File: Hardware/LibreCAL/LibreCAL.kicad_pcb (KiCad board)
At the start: 2 copper layers, 94 parts, among them J1 901-10510-2, J2 901-10510-2, J3 901-10510-2, J4 901-10510-2, J5 USB_C_Receptacle_USB2.0, J6 TC2030-ARM, Q1 IRLML2060, SW1 TL3301CF160QG, SW2 TL3301CF160QG, SW3 TL3301CF160QG, U1 PE426462, U2 PE426462, U3 PE426462, U4 PE426462, U5 W25Q16JVSNIQ, U6 IP4234CZ6, U7 RP2040, U8 W25Q16JVSNIQ, U9 MIC5528-3.3YMT-TR, Y1 ECS-120-8-36-CKM-TR3

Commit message: Partial routing
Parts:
- removed R10, R11: 13, Resistor_SMD:R_2512_6332Metric
- D1, D10, D11, D2, D3, D4, D5, D6, D7, D8, D9, J6, R14, R15, R16, R17, R18, R19, R20, R21, R22, R23, R24, SW1, SW2, SW3, TH1: moved to B.Cu
- R8, R9: value 13 -> 6R2; moved to B.Cu
- moved C30 97.4 mm to (119.6, 135.3), turned to -90 degrees
- moved C32 96.7 mm to (115.8, 135.3), turned to 90 degrees
- moved C28 93.9 mm to (121.6, 135.3), turned to -90 degrees
- moved C31 93.8 mm to (116.8, 135.3), turned to 90 degrees
- moved FB2 90.5 mm to (121.6, 133.4), turned to -90 degrees
- moved U9 89.8 mm to (118.2, 135.3), turned to 90 degrees
- moved C29 89.8 mm to (120.6, 135.3), turned to -90 degrees
- moved Q1 78.3 mm to (120.7, 121.0), turned to 180 degrees
- moved D6 76.8 mm to (109.0, 113.0), turned to 90 degrees
- moved C27 76.7 mm to (121.2, 123.7), turned to -90 degrees
- moved R18 75.4 mm to (115.0, 113.8)
- moved R19 74.7 mm to (111.0, 113.8)
- moved D7 73.8 mm to (105.0, 113.0), turned to 90 degrees
- moved SW3 73.6 mm to (110.0, 129.5), turned to 90 degrees
- moved R17 71.0 mm to (119.0, 113.8)
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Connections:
- U1 pad 20: unconnected-(U1-Pad20) -> GND
- U2 pad 20: unconnected-(U2-Pad20) -> GND
- U3 pad 2: Net-(U1-Pad15) -> Net-(U2-Pad2)
- U3 pad 20: unconnected-(U3-Pad20) -> GND
- U3 pad 4: Net-(U2-Pad4) -> Net-(U1-Pad15)
- U4 pad 15: Net-(U2-Pad2) -> Net-(U2-Pad4)
- U4 pad 20: unconnected-(U4-Pad20) -> GND
- U6 pad 1: Net-(J5-PadA7) -> Net-(J5-PadA6)
- U6 pad 6: Net-(J5-PadA6) -> Net-(J5-PadA7)
- U7 pad 11: P2_V2 -> LED_PORT4
- U7 pad 12: P2_V3 -> P3_V3
- U7 pad 13: P3_V1 -> P3_V2
- U7 pad 14: P3_V2 -> P3_V1
- U7 pad 15: P3_V3 -> P4_V1
- U7 pad 16: P4_V1 -> P4_V2
- U7 pad 17: P4_V2 -> P4_V3
- U7 pad 18: P4_V3 -> P2_V3
- U7 pad 27: LED_READY -> P2_V2
- U7 pad 28: LED_WAIT -> P2_V1
- U7 pad 29: LED_OPEN -> P1_V1
- U7 pad 30: LED_SHORT -> P1_V2
- U7 pad 31: LED_LOAD -> P1_V3
- U7 pad 32: LED_THROUGH -> LED_PORT1
- U7 pad 34: LED_PORT1 -> LED_PORT3
- U7 pad 35: LED_PORT2 -> LED_OPEN
- U7 pad 36: LED_PORT3 -> LED_SHORT
- U7 pad 37: LED_PORT4 -> LED_LOAD
- U7 pad 38: ADC_TEMP -> LED_THROUGH
- U7 pad 40: BUTTON1 -> HEATER
- U7 pad 41: HEATER -> ADC_TEMP
- U7 pad 46: Net-(U6-Pad3) -> Net-(U6-Pad4)
- U7 pad 47: Net-(U6-Pad4) -> Net-(U6-Pad3)
- U7 pad 6: P1_V1 -> BUTTON1
- U7 pad 7: P1_V2 -> LED_READY
- U7 pad 8: P1_V3 -> LED_WAIT
- U7 pad 9: P2_V1 -> LED_PORT2
- Y1 pad 4: (no net) -> GND
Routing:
- net GND: track 0.00 -> 179.0 mm, vias 0 -> 886
- net +3V3: track 0.00 -> 156.4 mm, vias 0 -> 18
- net P3_V3: track 0.00 -> 80.2 mm, vias 0 -> 2
- net P3_V2: track 0.00 -> 79.9 mm, vias 0 -> 2
- net P2_V3: track 0.00 -> 68.8 mm, vias 0 -> 2
- net P1_V3: track 0.00 -> 68.1 mm, vias 0 -> 2
- net P2_V1: track 0.00 -> 67.1 mm, vias 0 -> 2
- net P2_V2: track 0.00 -> 64.8 mm, vias 0 -> 2
- net P1_V2: track 0.00 -> 63.6 mm, vias 0 -> 2
- net P1_V1: track 0.00 -> 61.8 mm, vias 0 -> 2
- net Net-(R12-Pad2): track 0.00 -> 61.0 mm, vias 0 -> 2
- net P3_V1: track 0.00 -> 53.7 mm, vias 0 -> 2
- net LED_PORT2: track 0.00 -> 48.5 mm, vias 0 -> 2
- net LED_PORT1: track 0.00 -> 46.4 mm, vias 0 -> 2
- net P4_V1: track 0.00 -> 41.9 mm, vias 0 -> 2
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- added copper zone on B.Cu, net GND
- added copper zone on F.Cu, net GND
- added copper zone on In1.Cu, net GND
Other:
- board outline added: 55 x 65.5 mm
- copper layers 2 -> 4

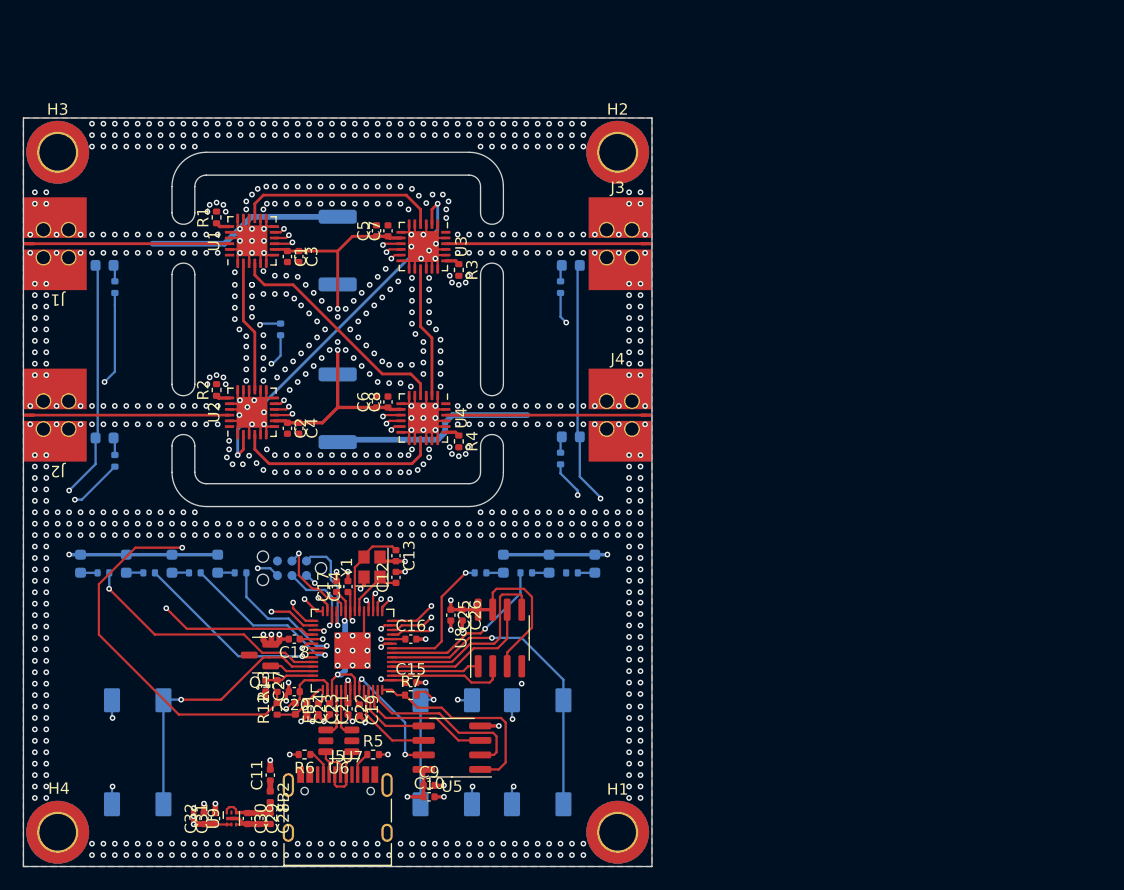
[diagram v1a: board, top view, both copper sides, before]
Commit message: Filters added, housing updated
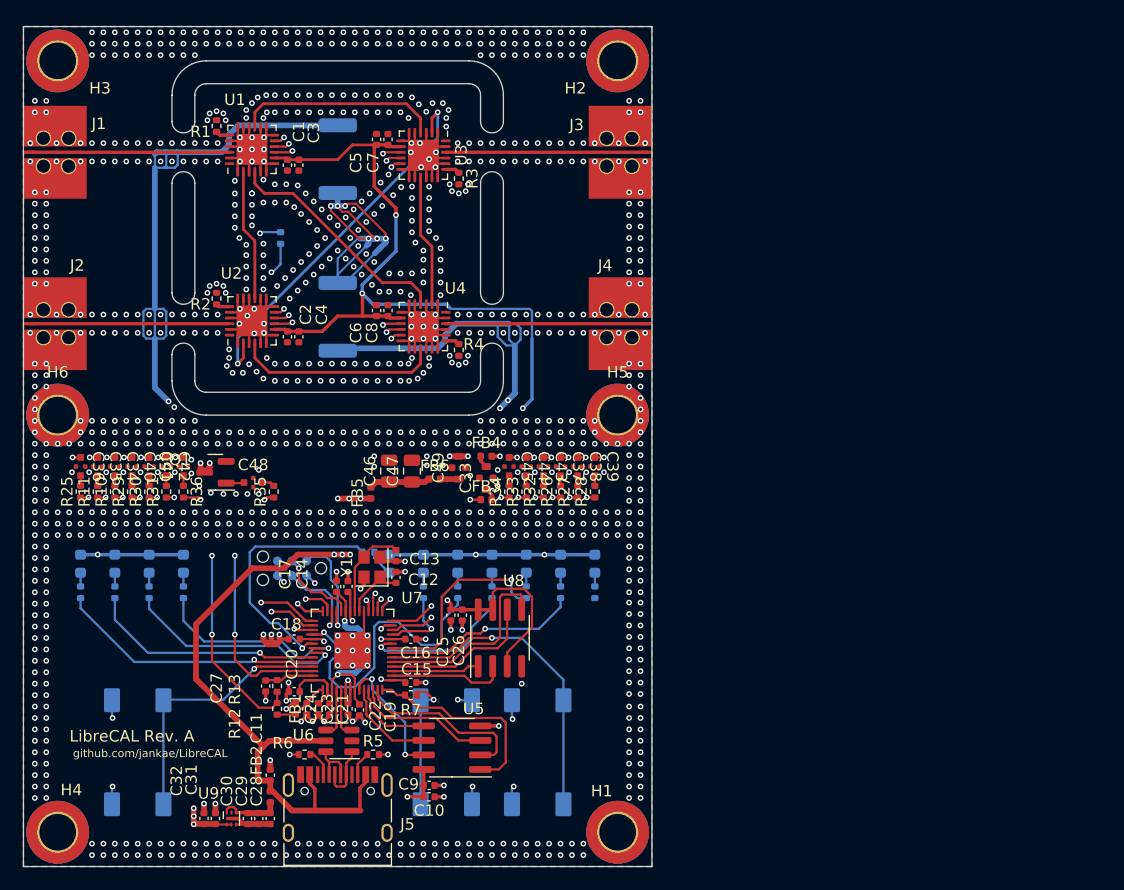
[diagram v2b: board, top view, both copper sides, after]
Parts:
- added C33: NFM21PC475B1A3D, LibreCAL:NFM21PC, F.Cu at (140.5, 105.5)
- added C34: NFM18CC223R1C3D, LibreCAL:NFM18CC, F.Cu at (108.0, 104.5)
- added C35: NFM18CC223R1C3D, LibreCAL:NFM18CC, F.Cu at (106.5, 104.5)
- added C36: NFM18CC223R1C3D, LibreCAL:NFM18CC, F.Cu at (105.0, 104.5)
- added C37: NFM18CC223R1C3D, LibreCAL:NFM18CC, F.Cu at (147.0, 104.5)
- added C38: NFM18CC223R1C3D, LibreCAL:NFM18CC, F.Cu at (148.5, 104.5)
- added C39: NFM18CC223R1C3D, LibreCAL:NFM18CC, F.Cu at (150.0, 104.5)
- added C40: NFM18CC223R1C3D, LibreCAL:NFM18CC, F.Cu at (109.5, 104.5)
- added C41: NFM18CC223R1C3D, LibreCAL:NFM18CC, F.Cu at (111.0, 104.5)
- added C42: NFM18CC223R1C3D, LibreCAL:NFM18CC, F.Cu at (112.5, 104.5)
- added C43: NFM18CC223R1C3D, LibreCAL:NFM18CC, F.Cu at (145.5, 104.5)
- added C44: NFM18CC223R1C3D, LibreCAL:NFM18CC, F.Cu at (144.0, 104.5)
- added C45: NFM18CC223R1C3D, LibreCAL:NFM18CC, F.Cu at (142.5, 104.5)
- added C46: 22u, Capacitor_SMD:C_0805_2012Metric, F.Cu at (132.0, 104.9)
- added C47: 22u, Capacitor_SMD:C_0805_2012Metric, F.Cu at (134.0, 104.9)
- added C48: NFM18CC223R1C3D, LibreCAL:NFM18CC, F.Cu at (120.1, 105.9)
- added C49: NFM21PC475B1A3D, LibreCAL:NFM21PC, F.Cu at (138.1, 104.6)
- added C50: NFM18CC223R1C3D, LibreCAL:NFM18CC, F.Cu at (114.0, 104.5)
- added COVER1: Top Cover, LibreCAL:TopCover, B.Cu at (155.0, 139.5)
- added COVER2: Bottom Cover, LibreCAL:BottomCover, B.Cu at (155.0, 139.5)
- added FB3: MMZ1005A222ET000, Inductor_SMD:L_0402_1005Metric, F.Cu at (140.5, 107.4)
- added FB4: MMZ1005A222ET000, Inductor_SMD:L_0402_1005Metric, F.Cu at (140.5, 103.6)
- added FB5: MMZ1005S121CTD25, Inductor_SMD:L_0402_1005Metric, F.Cu at (130.4, 106.8)
- added FB6: MMZ1005S121CTD25, Inductor_SMD:L_0402_1005Metric, F.Cu at (136.0, 105.6)
- added H5: MountingHole_Pad, MountingHole:MountingHole_3.2mm_M3_ISO14580_Pad_TopBottom, F.Cu at (152.0, 100.0)
- added H6: MountingHole_Pad, MountingHole:MountingHole_3.2mm_M3_ISO14580_Pad_TopBottom, F.Cu at (103.0, 100.0)
- added R10: 47k, Resistor_SMD:R_0402_1005Metric, F.Cu at (108.0, 106.7)
- added R11: 47k, Resistor_SMD:R_0402_1005Metric, F.Cu at (106.5, 106.7)
- added R25: 47k, Resistor_SMD:R_0402_1005Metric, F.Cu at (105.0, 106.7)
- added R26: 47k, Resistor_SMD:R_0402_1005Metric, F.Cu at (147.0, 106.7)
- added R27: 47k, Resistor_SMD:R_0402_1005Metric, F.Cu at (148.5, 106.7)
- added R28: 47k, Resistor_SMD:R_0402_1005Metric, F.Cu at (150.0, 106.7)
- added R29: 47k, Resistor_SMD:R_0402_1005Metric, F.Cu at (109.5, 106.7)
- added R30: 47k, Resistor_SMD:R_0402_1005Metric, F.Cu at (111.0, 106.7)
- added R31: 47k, Resistor_SMD:R_0402_1005Metric, F.Cu at (112.5, 106.7)
- added R32: 47k, Resistor_SMD:R_0402_1005Metric, F.Cu at (145.5, 106.7)
- added R33: 47k, Resistor_SMD:R_0402_1005Metric, F.Cu at (144.0, 106.7)
- added R34: 47k, Resistor_SMD:R_0402_1005Metric, F.Cu at (142.5, 106.7)
- added R35: 47k, Resistor_SMD:R_0402_1005Metric, F.Cu at (121.9, 106.7)
- added R36: 100, Resistor_SMD:R_0402_1005Metric, F.Cu at (114.0, 106.7)
- moved D8 40.4 mm to (138.0, 113.0), turned to 90 degrees
- moved R21 40.2 mm to (138.0, 115.5)
- moved R22 27.4 mm to (141.0, 115.5)
- moved D10 27.2 mm to (132.0, 113.0), turned to 90 degrees
- moved D9 27.0 mm to (141.0, 113.0), turned to 90 degrees
- moved R23 23.6 mm to (130.2, 112.0), turned to 180 degrees
- moved D11 17.0 mm to (135.0, 113.0), turned to 90 degrees
- moved R24 16.8 mm to (135.0, 115.5)
- moved Q1 16.5 mm to (116.8, 105.0)
- moved C1 8.00 mm to (123.1, 78.1)
- moved C2 8.00 mm to (123.1, 93.2)
- moved C3 8.00 mm to (124.1, 78.1)
- moved C4 8.00 mm to (124.1, 93.2)
- moved C5 8.00 mm to (130.9, 75.9)
- moved C6 8.00 mm to (130.9, 90.8)
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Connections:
- C1 pad 1: +3V3 -> Net-(C6-Pad1)
- C2 pad 1: +3V3 -> Net-(C6-Pad1)
- C3 pad 1: +3V3 -> Net-(C6-Pad1)
- C4 pad 1: +3V3 -> Net-(C6-Pad1)
- C5 pad 1: +3V3 -> Net-(C6-Pad1)
- C6 pad 1: +3V3 -> Net-(C6-Pad1)
- C7 pad 1: +3V3 -> Net-(C6-Pad1)
- C8 pad 1: +3V3 -> Net-(C6-Pad1)
- Q1 pad 1: HEATER -> Net-(Q1-Pad1)
- R12 pad 2: Net-(R12-Pad2) -> Net-(R13-Pad1)
- R13 pad 1: Net-(R12-Pad2) -> Net-(R13-Pad1)
- R21 pad 2: LED_PORT1 -> LED_PORT2
- R22 pad 2: LED_PORT2 -> LED_PORT1
- R23 pad 2: LED_PORT3 -> LED_PORT4
- R24 pad 2: LED_PORT4 -> LED_PORT3
- R8 pad 1: +5V -> Net-(R8-Pad1)
- TH1 pad 1: Net-(R12-Pad2) -> Net-(C50-Pad3)
- U1 pad 10: P1_V2 -> Net-(U1-Pad10)
- U1 pad 11: P1_V3 -> Net-(U1-Pad11)
- U1 pad 8: +3V3 -> Net-(C6-Pad1)
- U1 pad 9: P1_V1 -> Net-(U1-Pad9)
- U2 pad 10: P3_V2 -> Net-(U2-Pad10)
- U2 pad 11: P3_V3 -> Net-(U2-Pad11)
- U2 pad 8: +3V3 -> Net-(C6-Pad1)
- U2 pad 9: P3_V1 -> Net-(U2-Pad9)
- U3 pad 10: P2_V2 -> Net-(U3-Pad10)
- U3 pad 11: P2_V3 -> Net-(U3-Pad11)
- U3 pad 8: +3V3 -> Net-(C6-Pad1)
- U3 pad 9: P2_V1 -> Net-(U3-Pad9)
- U4 pad 10: P4_V2 -> Net-(U4-Pad10)
- U4 pad 11: P4_V3 -> Net-(U4-Pad11)
- U4 pad 8: +3V3 -> Net-(C6-Pad1)
- U4 pad 9: P4_V1 -> Net-(U4-Pad9)
- U7 pad 11: LED_PORT4 -> LED_PORT3
- U7 pad 12: P3_V3 -> P4_V3
- U7 pad 13: P3_V2 -> P4_V2
- U7 pad 14: P3_V1 -> P4_V1
- U7 pad 15: P4_V1 -> P3_V1
- U7 pad 16: P4_V2 -> P3_V2
- U7 pad 17: P4_V3 -> P3_V3
- U7 pad 18: P2_V3 -> P1_V3
- U7 pad 27: P2_V2 -> P1_V2
- U7 pad 28: P2_V1 -> P1_V1
- U7 pad 29: P1_V1 -> P2_V1
- U7 pad 30: P1_V2 -> P2_V2
- U7 pad 31: P1_V3 -> P2_V3
- U7 pad 32: LED_PORT1 -> LED_PORT2
- U7 pad 34: LED_PORT3 -> LED_PORT4
- U7 pad 9: LED_PORT2 -> LED_PORT1
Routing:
- net +3V3: track 156.4 -> 80.5 mm, vias 18 -> 16
- net Net-(Q1-Pad3): track 0.00 -> 73.5 mm, vias 0 -> 4
- net Net-(C6-Pad1): track 0.00 -> 71.3 mm, vias 0 -> 4
- net Net-(U2-Pad11): track 0.00 -> 63.1 mm, vias 0 -> 2
- net +5V: track 19.0 -> 81.0 mm, vias 0 -> 6
- net Net-(R12-Pad2): track 61.0 -> 0.00 mm, vias 2 -> 0
- net Net-(U2-Pad10): track 0.00 -> 60.2 mm, vias 0 -> 2
- net P3_V3: track 80.2 -> 20.3 mm
- net P3_V2: track 79.9 -> 20.3 mm
- net Net-(R8-Pad1): track 0.00 -> 51.4 mm, vias 0 -> 4
- net Net-(U3-Pad9): track 0.00 -> 49.2 mm, vias 0 -> 2
- net Net-(U3-Pad10): track 0.00 -> 46.6 mm, vias 0 -> 2
- net Net-(U1-Pad11): track 0.00 -> 46.3 mm, vias 0 -> 2
- net Net-(U3-Pad11): track 0.00 -> 45.0 mm, vias 0 -> 2
- net Net-(U1-Pad10): track 0.00 -> 44.2 mm, vias 0 -> 2
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- added copper zone on In2.Cu, net +3V3
- added copper zone on In2.Cu, net GND
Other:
- board size 55 x 65.5 mm -> 55 x 73.5 mm
- board text added: "BOOTSEL"
- board text added: "FUNCTION"
- board text added: "LOAD"
- board text added: "LibreCAL Rev. A"
- board text added: "OPEN"
- board text added: "PORT"
- board text added: "PORT1"
- board text added: "PORT2"
- board text added: "PORT3"
- board text added: "PORT4"
- board text added: "POWER"
- board text added: "READY"
- board text added: "SHORT"
- board text added: "THROUGH"
- board text added: "WAIT"
- board text added: "github.com/jankae/LibreCAL"

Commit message: Production files
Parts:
- COVER2: moved to F.Cu
- moved COVER2 57.5 mm to (97.5, 139.5), turned to 0 degrees
- moved COVER1 2.50 mm to (157.5, 139.5)
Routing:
- net GND: track 160.5 -> 172.9 mm, vias 1081 -> 1065

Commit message: replaced bootsel switch, adjusted covers
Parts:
- SW1: value TL3301CF160QG -> TL3301NF160QG; footprint LibreCAL:TL3301-J -> LibreCAL:TL3301N-J
- SW2, SW3: footprint LibreCAL:TL3301-J -> LibreCAL:TL3301C-J

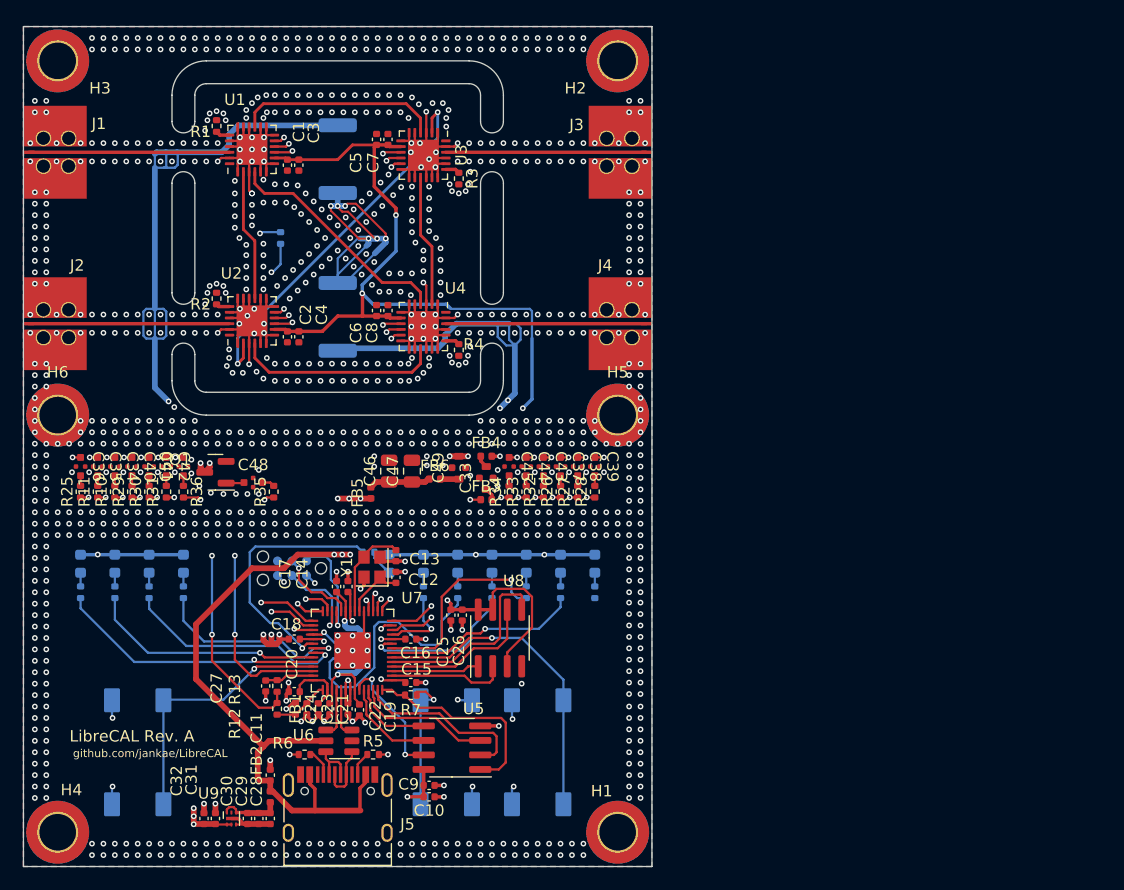
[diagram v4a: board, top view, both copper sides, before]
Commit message: Improvements on LibreCAL KiCad: fixed minor errors/labels(cosmetic), improved BOM(Added LCSC_Part), improved Impedance JLCPCB 4Layer JLC7628 1.6mm
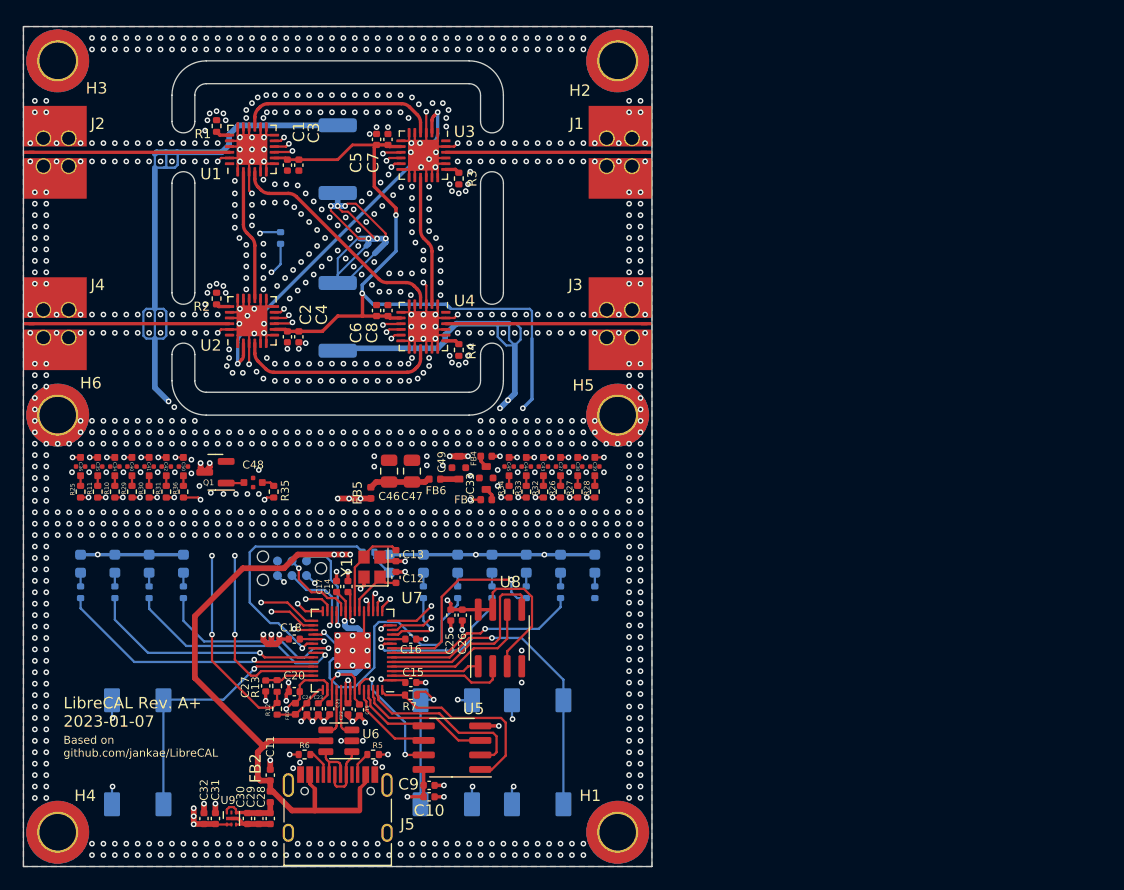
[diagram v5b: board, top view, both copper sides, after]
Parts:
- R1, R2, R3, R4: value 49R9 -> CH0402-50RGFTA
- renumbered J3 to J1, J1 to J2, J4 to J3, J2 to J4
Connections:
- net Net-(J1-Pad1) renamed /PortSwitch/U1_RFC_J2
- net Net-(J2-Pad1) renamed /PortSwitch/U2_RFC_J4
- net Net-(J3-Pad1) renamed /PortSwitch/U3_RFC_J1
- net Net-(J4-Pad1) renamed /PortSwitch/U4_RFC_J3
- net Net-(U1-Pad15) renamed /PortSwitch/U1_RF4_U3_RF3
- net Net-(U1-Pad2) renamed /PortSwitch/U1_RF2_U2_RF4
- net Net-(U1-Pad4) renamed /PortSwitch/U1_RF3_U4_RF3
- net Net-(U2-Pad2) renamed /PortSwitch/U3_RF2_U2_RF2
- net Net-(U2-Pad4) renamed /PortSwitch/U2_RF3_U4_RF4
- net Net-(U3-Pad15) renamed /PortSwitch/U3_RF4_U4_RF2
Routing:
- net GND: track 172.9 -> 185.6 mm, vias 1065 -> 1077
- net Net-(C39-Pad1): track 63.1 -> 62.5 mm
- net LED_PORT2: track 27.6 -> 27.1 mm
- net Net-(C40-Pad1): track 49.2 -> 48.6 mm
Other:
- board text added: "Based on github.com/jankae/LibreCAL"
- board text added: "JLCPCB 4Layer JLC7628 1.6mm Z50Ohms Track width 0.295mm"
- board text added: "LibreCAL Rev. ${REVISION} ${ISSUE_DATE}"
- board text removed: "LibreCAL Rev. A"
- board text removed: "github.com/jankae/LibreCAL"
